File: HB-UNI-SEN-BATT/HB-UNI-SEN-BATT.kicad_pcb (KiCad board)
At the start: 2 copper layers, 75 x 75 mm, 30 parts, among them J0 BATT, J1 I2C_1, J2 I2C_2, J3 A0, J4 A1, J5 A2, J6 A3, J7 PROG, J8 NO, Q1 IRLU024N, SW1 CONFIG_BUTTON, U1 ArduinoProMini, U2 CC1101

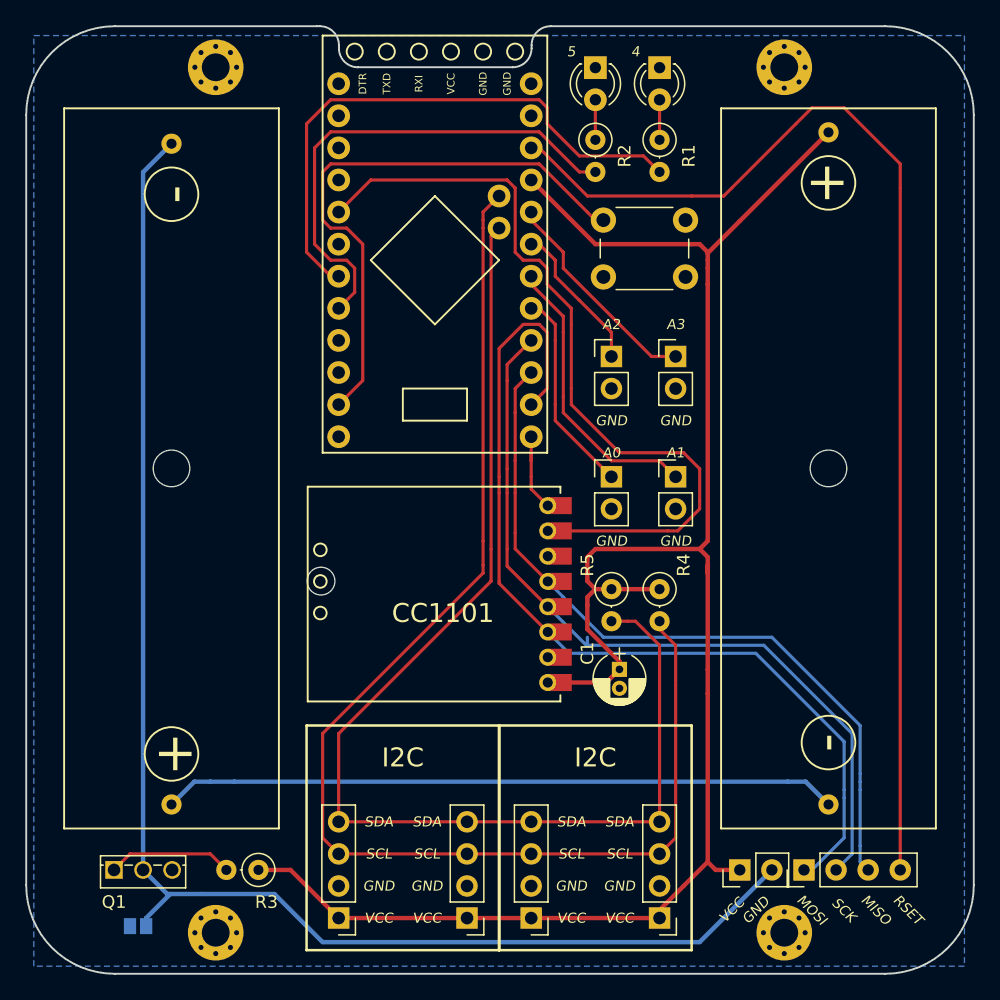
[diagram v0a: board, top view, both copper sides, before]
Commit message: Added new PCB HB-UNI-644, removed unfinished HB-UNI-SEN-O
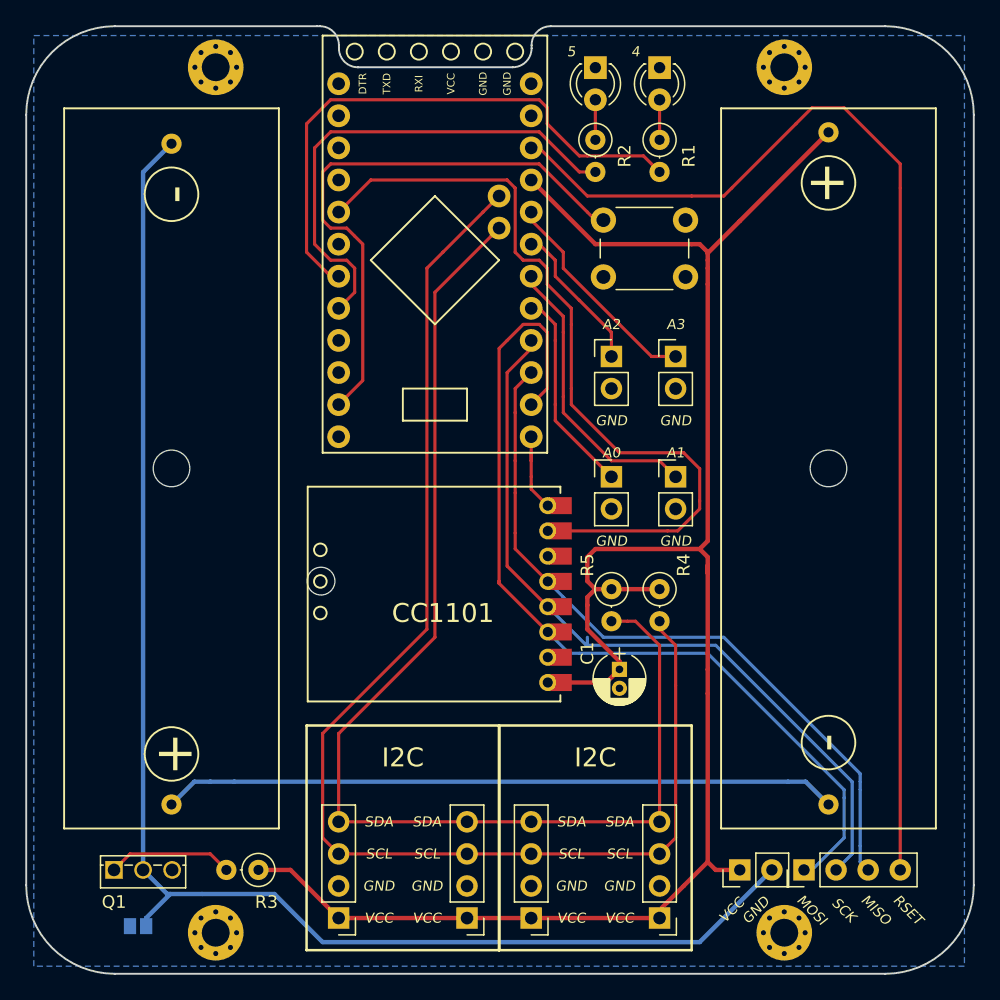
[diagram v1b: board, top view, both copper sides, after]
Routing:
- net /MISO: track 60.3 -> 58.0 mm
- net /SCK: track 64.4 -> 62.2 mm
- net /MOSI: track 75.0 -> 73.2 mm
- net /SDA: track 96.9 -> 97.8 mm
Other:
- board text added: "Version 1.6 - 05/2018"
- board text removed: "Version 1.5 - 05/2018"

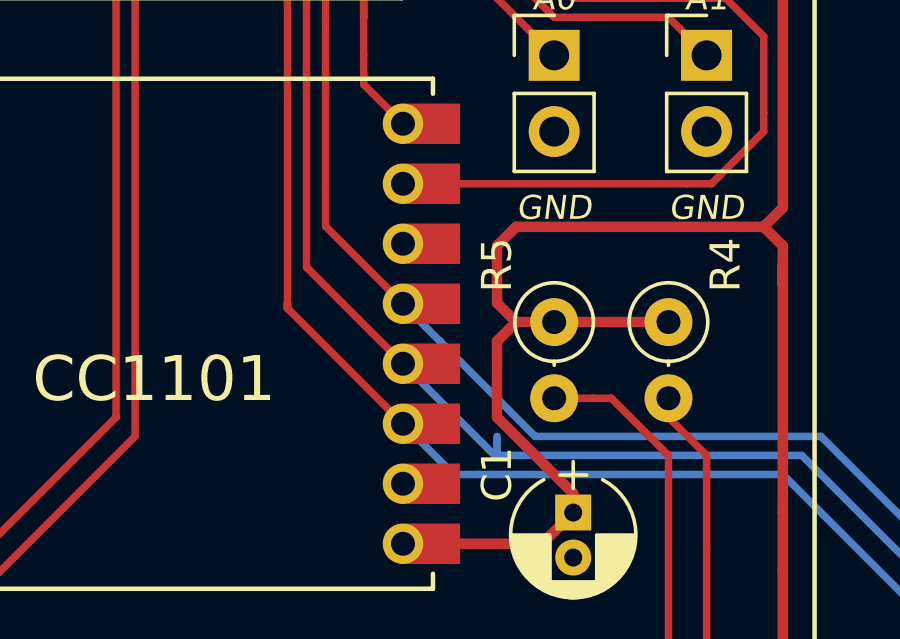
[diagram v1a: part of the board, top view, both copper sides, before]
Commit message: Fixed Gerber files of HB-UNI-SEN-BATT (fixes #2)
Fixed README of HB-UNI-BATT (fixes #1)
Optimized Silkscreen of HB-UNI-644
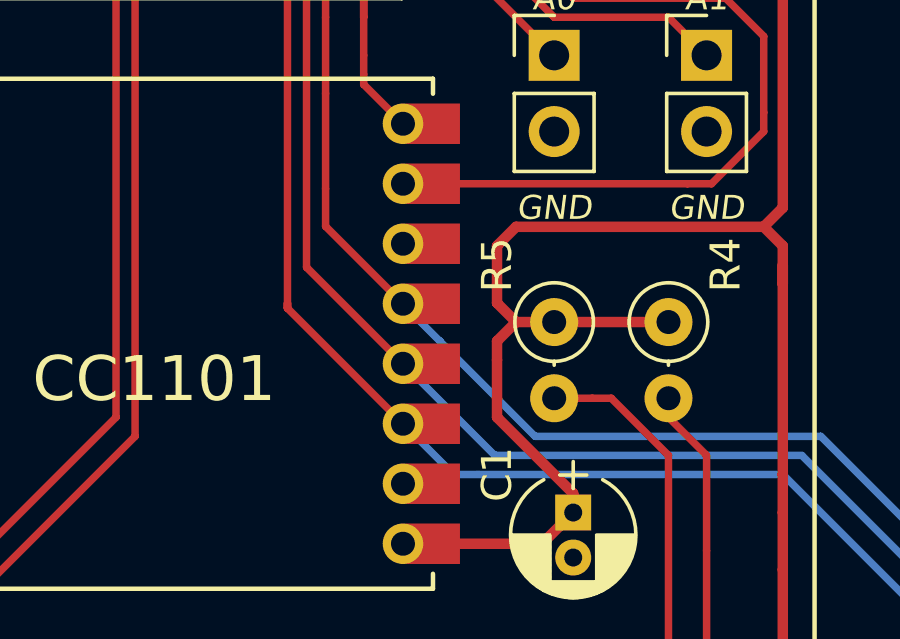
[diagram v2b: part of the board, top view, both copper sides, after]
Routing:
- net /D2: track 63.2 -> 64.2 mm
- net /SCK: track 62.2 -> 61.5 mm
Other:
- board text added: "Version 1.7 - 07/2018"
- board text removed: "Version 1.6 - 05/2018"
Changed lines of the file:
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@@
   (general
     (links 69)
-    (no_connects 1)
-    (area 100.924999 77.924999 176.075001 153.075001)
+    (no_connects 0)
+    (area 100.924999 77.075 176.075001 154.025)
     (thickness 1.6)
     (drawings 63)
@@
     (effects (font (size 1.2 1.2) (thickness 0.2)) (justify left mirror))
   )
-  (gr_text "Version 1.6 - 05/2018\n" (at 109.22 90.17 90) (layer B.SilkS)
+  (gr_text "Version 1.7 - 07/2018\n" (at 109.22 90.17 90) (layer B.SilkS)
     (effects (font (size 1.2 1.2) (thickness 0.2)) (justify left mirror))
   )
@@
   (segment (start 140.97 112.395) (end 140.97 110.49) (width 0.25) (layer F.Cu) (net 11))
   (segment (start 140.97 111.76) (end 140.97 112.395) (width 0.25) (layer F.Cu) (net 11))
+  (segment (start 142.28 117.945) (end 143.28 117.945) (width 0.25) (layer F.Cu) (net 12))
   (segment (start 144.145 106.68) (end 144.145 107.95) (width 0.25) (layer F.Cu) (net 12))
   (segment (start 153.035 111.76) (end 154.305 113.03) (width 0.25) (layer F.Cu) (net 12))
@@
   (segment (start 145.415 127) (end 145.335 127) (width 0.25) (layer B.Cu) (net 20))
   (segment (start 145.335 127) (end 142.28 123.945) (width 0.25) (layer B.Cu) (net 20))
-  (segment (start 145.415 127) (end 145.415 126.365) (width 0.25) (layer B.Cu) (net 20))
   (segment (start 145.415 127) (end 155.575 127) (width 0.25) (layer B.Cu) (net 20))
   (segment (start 166.37 143.51) (end 165.1 144.78) (width 0.25) (layer B.Cu) (net 20))

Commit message: Relicened under CC BY-ND-SA
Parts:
- added G***: LOGO, Homebrew:CC-BY-ND-SA, B.Cu at (171.4, 134.0)
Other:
- board text added: "Version 1.8 - 08/2018"
- board text removed: "Version 1.7 - 07/2018"
